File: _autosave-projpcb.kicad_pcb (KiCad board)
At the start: 2 copper layers, 130 x 70 mm, 34 parts, among them CON1 BARREL_JACK, CON2 BARREL_JACK, P1 CONN_01X02, P2 CONN_01X02, Q1 SFH3711, Q10 SFH3711, Q11 SFH3711, Q12 SFH3711, Q13 SFH3711, Q14 SFH3711, Q15 SFH3711, Q16 Q_NMOS_GSD, Q2 SFH3711, Q3 SFH3711, Q4 SFH3711, Q5 SFH3711, Q6 SFH3711, Q7 SFH3711, Q8 SFH3711, Q9 SFH3711, U1 Teensy_3.1, U2 LM358, U3 CD74HC4067, U4 CL520

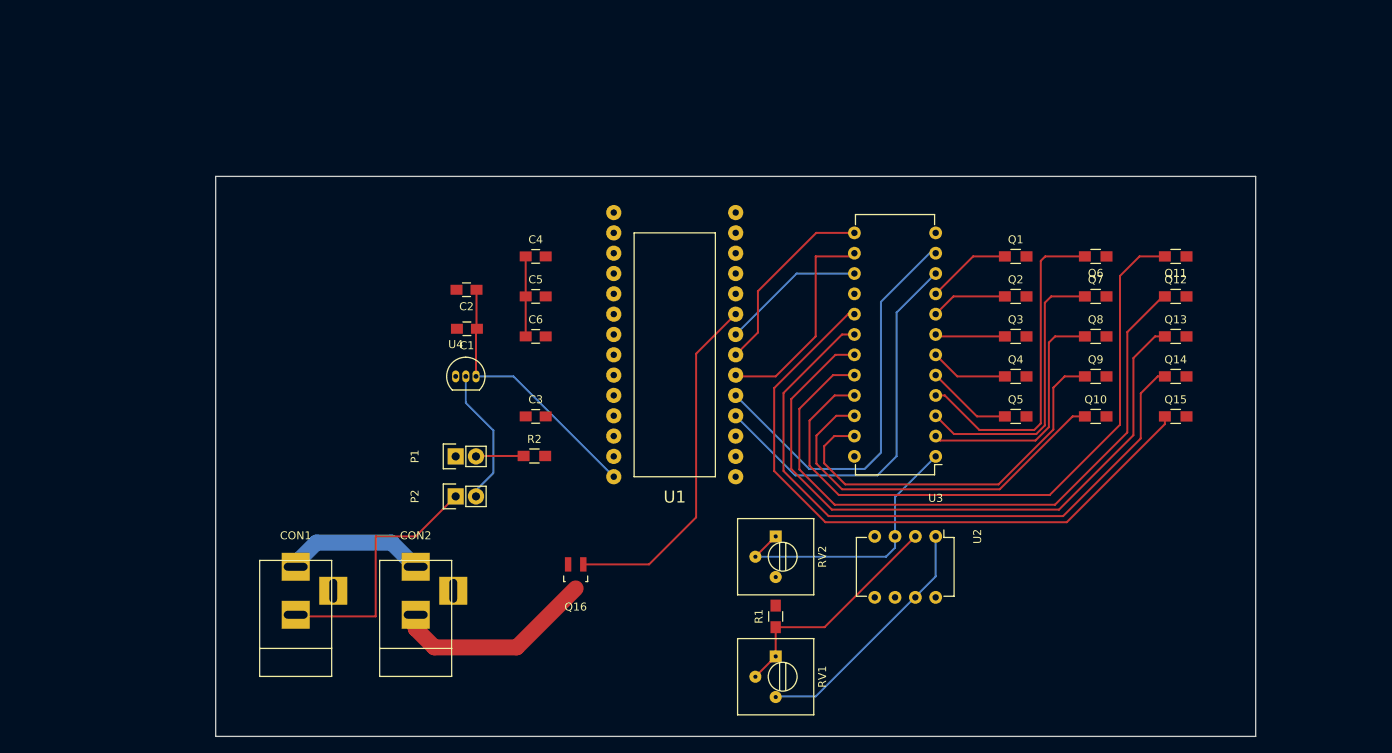
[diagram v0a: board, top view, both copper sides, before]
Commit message: Added breakout headers for phototransistors, added GNDA for analog aspects
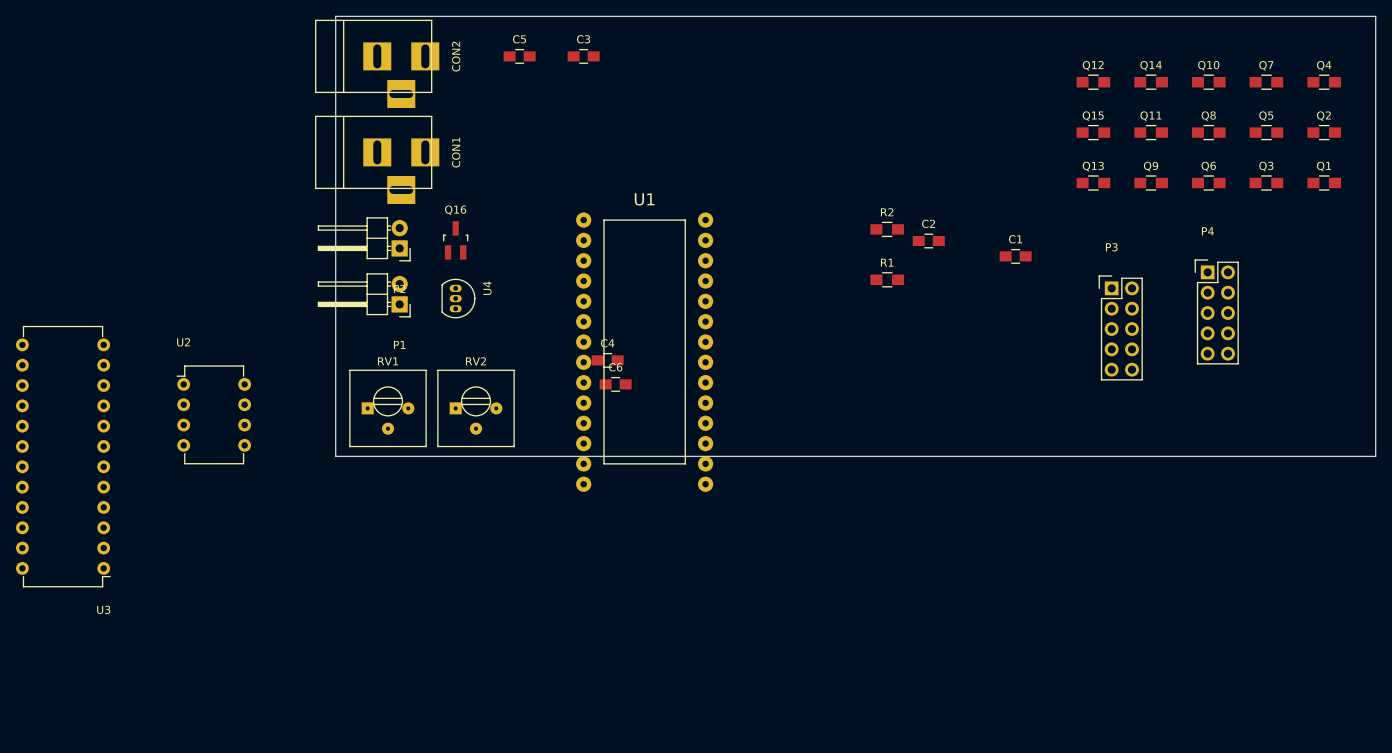
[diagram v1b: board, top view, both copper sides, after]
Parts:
- added P3: CONN_02X05, Pin_Headers:Pin_Header_Straight_2x05, F.Cu at (227.0, 109.0)
- added P4: CONN_02X05, Pin_Headers:Pin_Header_Straight_2x05, F.Cu at (239.0, 107.0)
- P1, P2: footprint Pin_Headers:Pin_Header_Straight_1x02 -> Pin_Headers:Pin_Header_Angled_1x02
- moved U3 104.9 mm to (101.0, 144.0)
- moved U2 95.9 mm to (111.0, 121.0), turned to 0 degrees
- moved CON2 70.2 mm to (135.0, 80.0), turned to 0 degrees
- moved C1 69.2 mm to (215.0, 105.0), turned to 0 degrees
- moved RV1 59.7 mm to (134.0, 124.0), turned to 0 degrees
- moved CON1 58.9 mm to (135.0, 92.0), turned to 0 degrees
- moved C2 58.1 mm to (204.1, 103.1), turned to 0 degrees
- moved Q4 53.3 mm to (253.6, 83.2)
- moved R2 52.4 mm to (198.9, 101.6)
- moved Q5 47.3 mm to (246.3, 89.5)
- moved C3 45.4 mm to (161.0, 80.0)
- moved Q16 44.6 mm to (145.0, 103.0), turned to 0 degrees
- moved R1 44.3 mm to (198.9, 107.9), turned to 0 degrees
- moved Q10 44.1 mm to (239.1, 83.2)
- moved Q2 43.7 mm to (253.6, 89.5)
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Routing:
- net /Phototransistors/S13: track 82.4 -> 0.00 mm
- net /Phototransistors/S14: track 82.2 -> 0.00 mm
- net /Phototransistors/S12: track 81.9 -> 0.00 mm
- net /Phototransistors/S15: track 81.8 -> 0.00 mm
- net /Phototransistors/S11: track 81.7 -> 0.00 mm
- net T3: track 51.0 -> 0.00 mm
- net /Phototransistors/S9: track 49.2 -> 0.00 mm
- net T2: track 49.1 -> 0.00 mm
- net /Phototransistors/S10: track 47.9 -> 0.00 mm
- net HEAT: track 44.0 -> 0.00 mm
- net /Phototransistors/S6: track 41.3 -> 0.00 mm
- net /Phototransistors/S7: track 35.7 -> 0.00 mm
- net Net-(RV2-Pad1): track 35.1 -> 0.00 mm
- net VIN: track 33.3 -> 0.00 mm
- net GND: track 32.3 -> 0.00 mm
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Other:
- board size 130 x 70 mm -> 130 x 55 mm
- rule pad_to_mask_clearance: 0.2 -> 0
